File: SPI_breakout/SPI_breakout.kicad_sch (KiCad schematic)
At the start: 2 parts

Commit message: AI assisted edits on board
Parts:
- added J1: OPC-N3 A, Connector_Phoenix_MC:PhoenixContact_MC_1,5_6-G-3.81_1x06_P3.81mm_Horizontal, symbol MyParts:AlphaSense_OPC_N3
- added J2: OPC-N3 B, Connector_Phoenix_MC:PhoenixContact_MC_1,5_6-G-3.81_1x06_P3.81mm_Horizontal, symbol MyParts:AlphaSense_OPC_N3
- added J3: External OPC 5V Input, Connector_Phoenix_MC:PhoenixContact_MC_1,5_2-G-3.81_1x02_P3.81mm_Horizontal, symbol MyParts:External_5V_Input
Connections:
- net SD_CS: now reaches U1.25 (SPI_CS), U2.6 (CS)
- net SPI_CLK: now reaches U1.26 (SPI_CLK), U2.3 (CLK)
- net SPI_CLK: now also J1.6 (SCK), J2.6 (SCK)
- net SPI_MISO: now reaches U1.27 (SPI_MISO), U2.4 (D0_SO)
- net SPI_MISO: now also J1.5 (SDO_MISO), J2.5 (SDO_MISO)
- net SPI_MOSI: now reaches U1.28 (SPI_MOSI), U2.5 (D1_CMD)
- net SPI_MOSI: now also J1.4 (SDI_MOSI), J2.4 (SDI_MOSI)
- net OPC1_CS: now reaches U1.29 (IO1)
- net OPC1_CS: now also J1.3 (SS)
- net OPC2_CS: now reaches U1.31 (IO3)
- net OPC2_CS: now also J2.3 (SS)
- net GND: now reaches U1.40 (GND), U2.2 (GND)
- net GND: now also J1.1 (GND), J2.1 (GND), J3.2 (GND)
- new net OPC_5V_EXT: J1.2 (5V_EXT), J2.2 (5V_EXT), J3.1 (5V_EXT)
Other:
- note added: "J1/J2 pin order: 1 GND black, 2 5V_EXT red, 3 SS green, 4 SDI blue, 5 SDO white, 6 SCK yellow. Use 3.81mm 6-pos pluggable terminals such as TJ0631030000G with a matching PCB header."
- note added: "J3 is the separate OPC 5V input. Pin 1 feeds only OPC_5V_EXT on J1/J2 pin 2; pin 2 ties that supply return to WisBlock GND. It is not tied to the WisBlock 3v3 rail."
- note added: "No level shifter fitted: WisBlock, SD reader, and OPC SPI are expected to use 3.3V logic. Verify OPC SPI adapter before 5V power-up."
- note added: "OPC-N3 5V+ is external; tie the OPC supply ground to WisBlock GND."

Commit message: Reworking routing
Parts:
- added GAS1, GAS2: Screw_Terminal_01x04, MyParts:CONN_1984633_PXC, symbol MyParts:Screw_Terminal_01x04
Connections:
- net GND: now also GAS1.2 (GND)
- net at U1.17 (3v3): now also GAS1.1 (VCC)
- net at U1.19 (SDA1): now also GAS1.4 (SDA)
- net at U1.20 (SCL1): now also GAS1.3 (SCL)
- net at U1.35 (SDA2): now also GAS2.4 (SDA)
- net at U1.36 (SCL2): now also GAS2.3 (SCL)
- net at U1.4 (GND): now also GAS2.2 (GND)
- net at U1.5 (3v3): now also GAS2.1 (VCC)

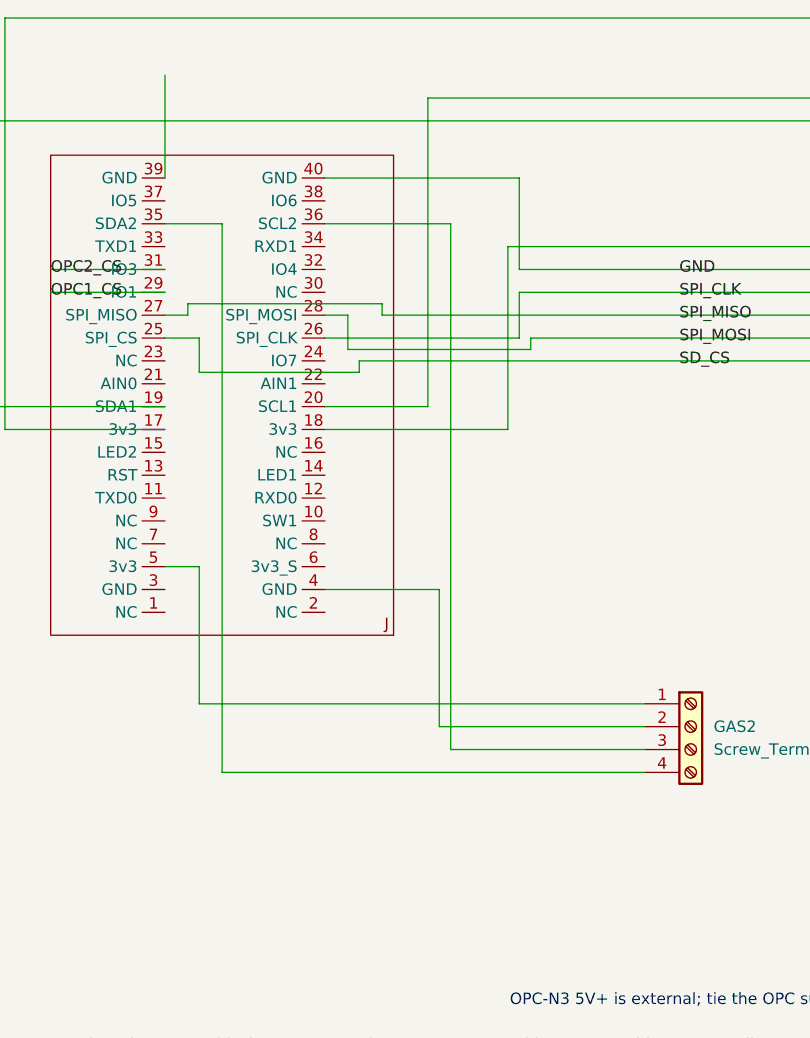
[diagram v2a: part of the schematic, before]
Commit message: Rework into smaller footprint and add 3D models
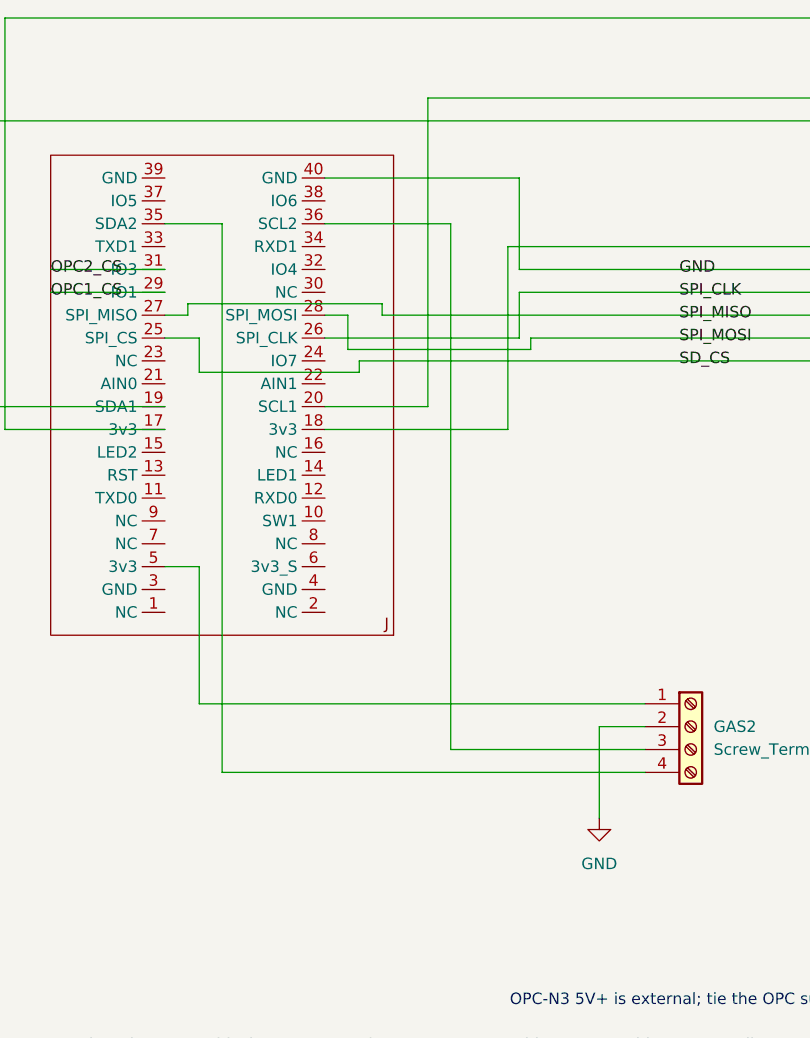
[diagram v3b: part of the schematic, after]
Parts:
- J1, J2: footprint Connector_Phoenix_MC:PhoenixContact_MC_1,5_6-G-3.81_1x06_P3.81mm_Horizontal -> MyParts:CONN_1984659_PXC
- J3: footprint Connector_Phoenix_MC:PhoenixContact_MC_1,5_2-G-3.81_1x02_P3.81mm_Horizontal -> MyParts:CONN_1935161_PXC
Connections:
- net GND: now also GAS2.2 (GND)
- net at U1.4 (GND): no longer GAS2.2 (GND)
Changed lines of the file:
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@@
-	(wire
-		(pts
-			(xy 93.98 93.98) (xy 81.28 93.98)
-		)
-		(stroke
-			(width 0)
-			(type default)
-		)
-	)
 	(wire
 		(pts
@@
 	(wire
 		(pts
-			(xy 63.5 36.83) (xy 63.5 48.26)
-		)
-		(stroke
-			(width 0)
-			(type default)
-		)
-	)
-	(wire
-		(pts
 			(xy 167.64 129.54) (xy 152.4 129.54)
 		)
@@
 	(wire
 		(pts
-			(xy 93.98 109.22) (xy 93.98 93.98)
-		)
-		(stroke
-			(width 0)
-			(type default)
-		)
-	)
-	(wire
-		(pts
 			(xy 63.5 76.2) (xy 45.72 76.2)
 		)
@@
 	(wire
 		(pts
+			(xy 111.76 109.22) (xy 111.76 119.38)
+		)
+		(stroke
+			(width 0)
+			(type default)
+		)
+	)
+	(wire
+		(pts
 			(xy 66.04 63.5) (xy 63.5 63.5)
 		)
@@
 	(wire
 		(pts
+			(xy 116.84 109.22) (xy 111.76 109.22)
+		)
+		(stroke
+			(width 0)
+			(type default)
+		)
+	)
+	(wire
+		(pts
 			(xy 95.25 53.34) (xy 81.28 53.34)
 		)
@@
 		(pts
 			(xy 167.64 55.88) (xy 101.6 55.88)
-		)
-		(stroke
-			(width 0)
-			(type default)
-		)
-	)
-	(wire
-		(pts
-			(xy 116.84 109.22) (xy 93.98 109.22)
 		)
 		(stroke
@@
 			(font
 				(size 1.27 1.27)
+			)
+		)
+	)
+	(symbol
+		(lib_id "power:GND")
+		(at 111.76 119.38 0)
+		(unit 1)
+		(body_style 1)
+		(exclude_from_sim no)
+		(in_bom yes)
+		(on_board yes)
+		(in_pos_files yes)
+		(dnp no)
+		(fields_autoplaced yes)
+		(property "Reference" "#PWR02"
+			(at 111.76 125.73 0)
+			(hide yes)
+			(show_name no)
+			(do_not_autoplace no)
+			(effects
+				(font
+					(size 1.27 1.27)
+				)
+			)
+		)
+		(property "Value" "GND"
+			(at 111.76 124.46 0)
+			(show_name no)
+			(do_not_autoplace no)
+			(effects
+				(font
+					(size 1.27 1.27)
+				)
+			)
+		)
+		(property "Footprint" ""
+			(at 111.76 119.38 0)
+			(hide yes)
+			(show_name no)
+			(do_not_autoplace no)
+			(effects
+				(font
+					(size 1.27 1.27)
+				)
+			)
+		)
+		(property "Datasheet" ""
+			(at 111.76 119.38 0)
+			(hide yes)
+			(show_name no)
+			(do_not_autoplace no)
+			(effects
+				(font
+					(size 1.27 1.27)
+				)
+			)
+		)
+		(property "Description" "Power symbol creates a global label with name \"GND\" , ground"
+			(at 111.76 119.38 0)
+			(hide yes)
+			(show_name no)
+			(do_not_autoplace no)
+			(effects
+				(font
+					(size 1.27 1.27)
+				)
+			)
+		)
+		(pin "1"
+		)
+		(instances
+			(project "SPI_breakout"
+				(path "/d8da890c-b85a-4ee7-8a35-6f5c92ac20f5"
+					(reference "#PWR02")
+					(unit 1)
+				)
 			)
 		)
@@
 			)
 		)
-		(property "Footprint" "Connector_Phoenix_MC:PhoenixContact_MC_1,5_6-G-3.81_1x06_P3.81mm_Horizontal"
+		(property "Footprint" "MyParts:CONN_1984659_PXC"
 			(at 167.64 86.36 0)
 			(hide yes)
@@
 			)
 		)
-		(property "Footprint" "Connector_Phoenix_MC:PhoenixContact_MC_1,5_6-G-3.81_1x06_P3.81mm_Horizontal"
+		(property "Footprint" "MyParts:CONN_1984659_PXC"
 			(at 167.64 114.3 0)
 			(hide yes)
@@
 			)
 		)
-		(property "Footprint" "Connector_Phoenix_MC:PhoenixContact_MC_1,5_2-G-3.81_1x02_P3.81mm_Horizontal"
+		(property "Footprint" "MyParts:CONN_1935161_PXC"
 			(at 167.64 157.48 0)
 			(hide yes)

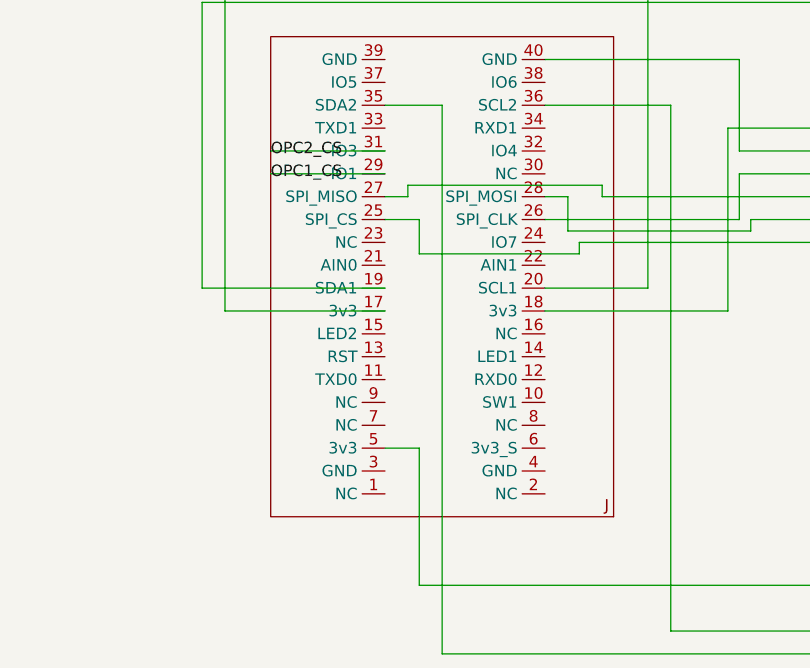
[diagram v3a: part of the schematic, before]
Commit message: Cleaning up routes
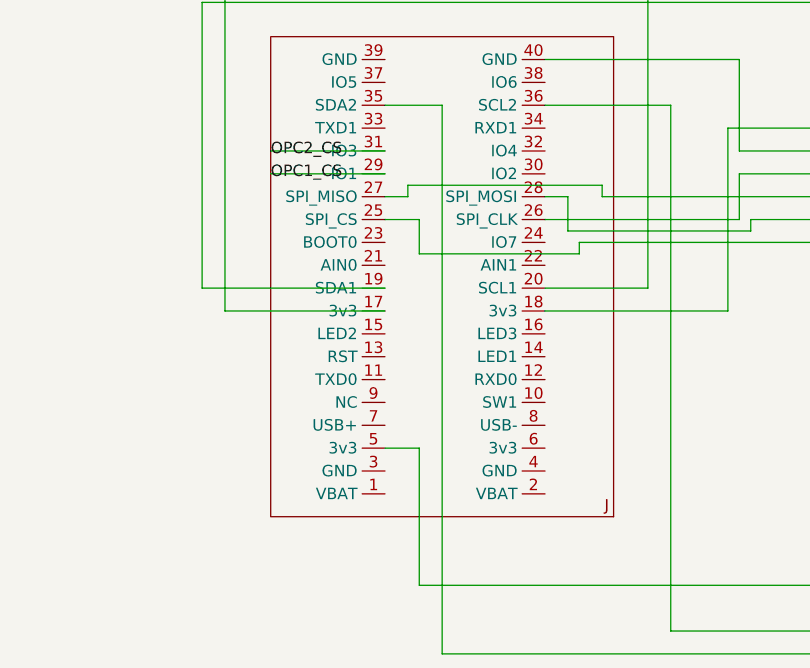
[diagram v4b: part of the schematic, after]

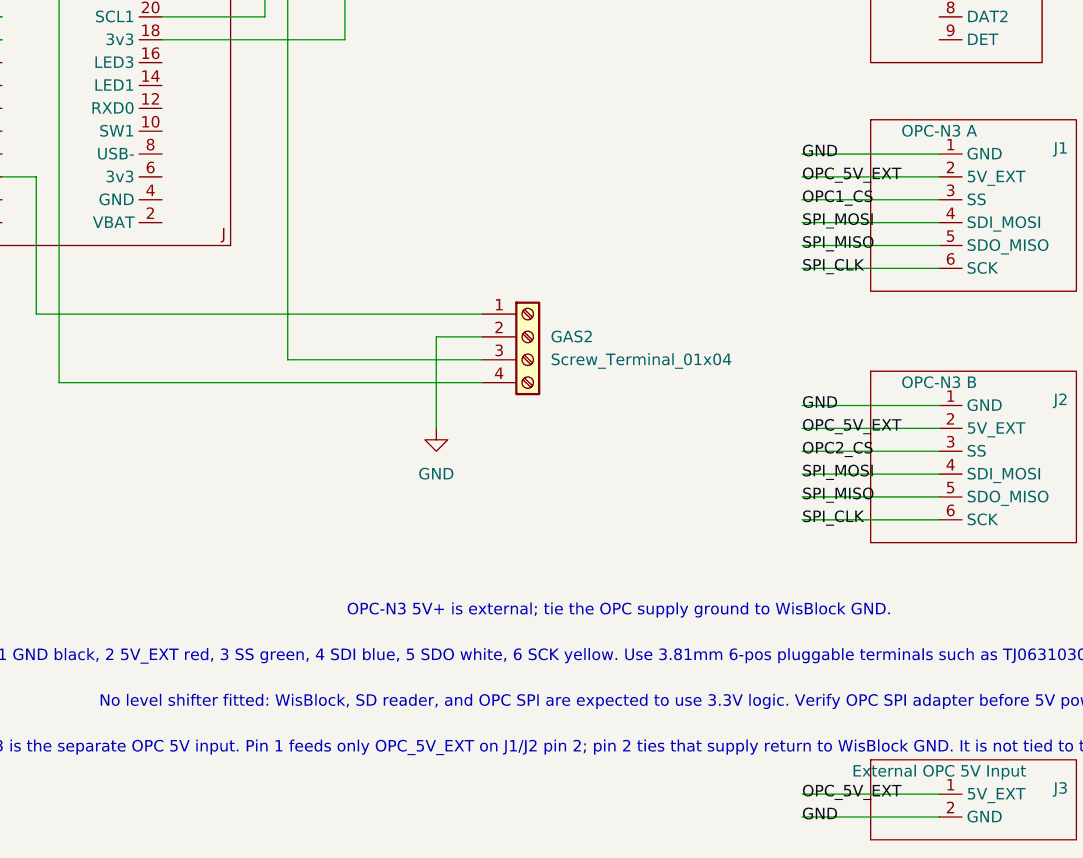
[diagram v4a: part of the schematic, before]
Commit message: Added power switching and bigger pad for SD mount
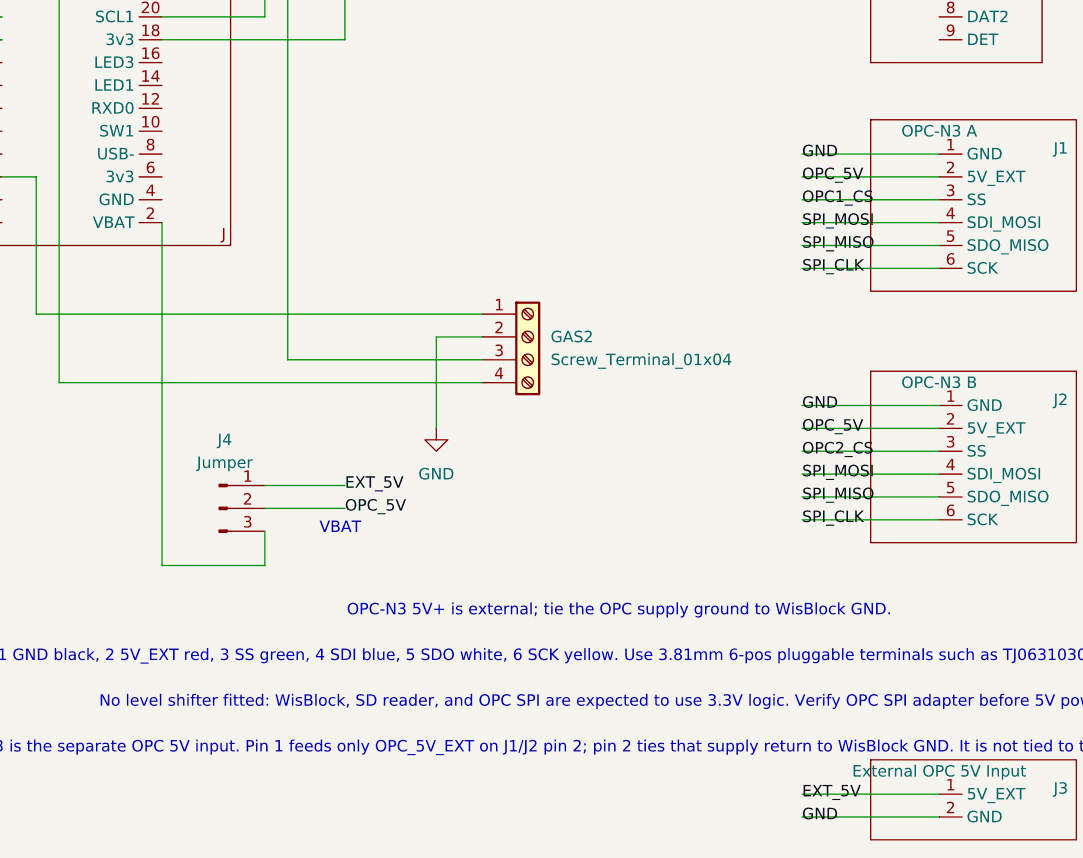
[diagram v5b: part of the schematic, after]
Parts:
- added J4: Jumper, Connector_PinHeader_2.54mm:PinHeader_1x03_P2.54mm_Vertical, symbol MyParts:Jumper
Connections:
- net at U1.2 (VBAT): now also J4.3 (VBAT)
- net OPC_5V_EXT renamed OPC_5V
- net OPC_5V: now also J4.2 (OPC_5V); no longer J3.1 (5V_EXT)
- new net EXT_5V: J3.1 (5V_EXT), J4.1 (EXT_5V)
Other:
- note added: "VBAT"
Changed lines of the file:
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@@
+		)
+	)
+	(text "VBAT"
+		(exclude_from_sim no)
+		(at 101.092 130.556 0)
+		(effects
+			(font
+				(size 1.27 1.27)
+				(color 0 0 0 1)
+			)
 		)
 	)
@@
 	(wire
 		(pts
+			(xy 92.71 134.62) (xy 92.71 130.81)
+		)
+		(stroke
+			(width 0)
+			(type default)
+		)
+	)
+	(wire
+		(pts
 			(xy 167.64 68.58) (xy 85.09 68.58)
 		)
@@
 	(wire
 		(pts
+			(xy 81.28 134.62) (xy 92.71 134.62)
+		)
+		(stroke
+			(width 0)
+			(type default)
+		)
+	)
+	(wire
+		(pts
 			(xy 167.64 66.04) (xy 104.14 66.04)
 		)
@@
 	(wire
 		(pts
+			(xy 92.71 125.73) (xy 101.6 125.73)
+		)
+		(stroke
+			(width 0)
+			(type default)
+		)
+	)
+	(wire
+		(pts
 			(xy 83.82 63.5) (xy 81.28 63.5)
 		)
@@
 	(wire
 		(pts
+			(xy 92.71 128.27) (xy 101.6 128.27)
+		)
+		(stroke
+			(width 0)
+			(type default)
+		)
+	)
+	(wire
+		(pts
 			(xy 83.82 67.31) (xy 83.82 63.5)
 		)
@@
 		(pts
 			(xy 43.18 41.91) (xy 43.18 73.66)
+		)
+		(stroke
+			(width 0)
+			(type default)
+		)
+	)
+	(wire
+		(pts
+			(xy 81.28 96.52) (xy 81.28 134.62)
 		)
 		(stroke
@@
 		)
 	)
+	(label "OPC_5V"
+		(at 101.6 128.27 0)
+		(effects
+			(font
+				(size 1.27 1.27)
+			)
+		)
+	)
 	(label "OPC1_CS"
 		(at 152.4 93.98 0)
@@
 		)
 	)
-	(label "OPC_5V_EXT"
+	(label "EXT_5V"
 		(at 152.4 160.02 0)
 		(effects
@@
 		)
 	)
-	(label "OPC_5V_EXT"
+	(label "OPC_5V"
 		(at 152.4 119.38 0)
 		(effects
@@
 		)
 	)
-	(label "OPC_5V_EXT"
+	(label "EXT_5V"
+		(at 101.6 125.73 0)
+		(effects
+			(font
+				(size 1.27 1.27)
+			)
+		)
+	)
+	(label "OPC_5V"
 		(at 152.4 91.44 0)
 		(effects
@@
 					(unit 1)
 				)
+			)
+		)
+	)
+	(symbol
+		(lib_id "MyParts:Jumper")
+		(at 87.63 128.27 0)
+		(unit 1)
+		(body_style 1)
+		(exclude_from_sim no)
+		(in_bom yes)
+		(on_board yes)
+		(in_pos_files yes)
+		(dnp no)
+		(fields_autoplaced yes)
+		(property "Reference" "J4"
+			(at 88.265 120.65 0)
+			(show_name no)
+			(do_not_autoplace no)
+			(effects
+				(font
+					(size 1.27 1.27)
+				)
+			)
+		)
+		(property "Value" "Jumper"
+			(at 88.265 123.19 0)
+			(show_name no)
+			(do_not_autoplace no)
+			(effects
+				(font
+					(size 1.27 1.27)
+				)
+			)
+		)
+		(property "Footprint" "Connector_PinHeader_2.54mm:PinHeader_1x03_P2.54mm_Vertical"
+			(at 87.63 128.27 0)
+			(hide yes)
+			(show_name no)
+			(do_not_autoplace no)
+			(effects
+				(font
+					(size 1.27 1.27)
+				)
+			)
+		)
+		(property "Datasheet" ""
+			(at 87.63 128.27 0)
+			(hide yes)
+			(show_name no)
+			(do_not_autoplace no)
+			(effects
+				(font
+					(size 1.27 1.27)
+				)
+			)
+		)
+		(property "Description" "01x03 Pin Jumper"
+			(at 98.552 122.936 0)
+			(hide yes)
+			(show_name no)
+			(do_not_autoplace no)
+			(effects
+				(font
+					(size 1.27 1.27)
+				)
+			)
+		)
+		(pin "1"
+		)
+		(pin "2"
+		)
+		(pin "3"
+		)
+		(instances
+			(project "SPI_breakout"
+				(path "/d8da890c-b85a-4ee7-8a35-6f5c92ac20f5"
+					(reference "J4")
+					(unit 1)
+				)

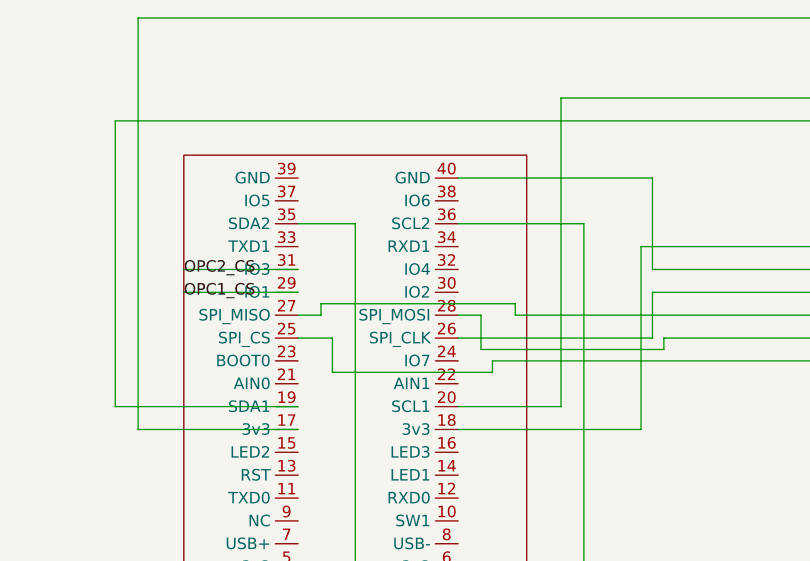
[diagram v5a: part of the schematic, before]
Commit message: Change IO pin to 2 to avoid GPS conflict
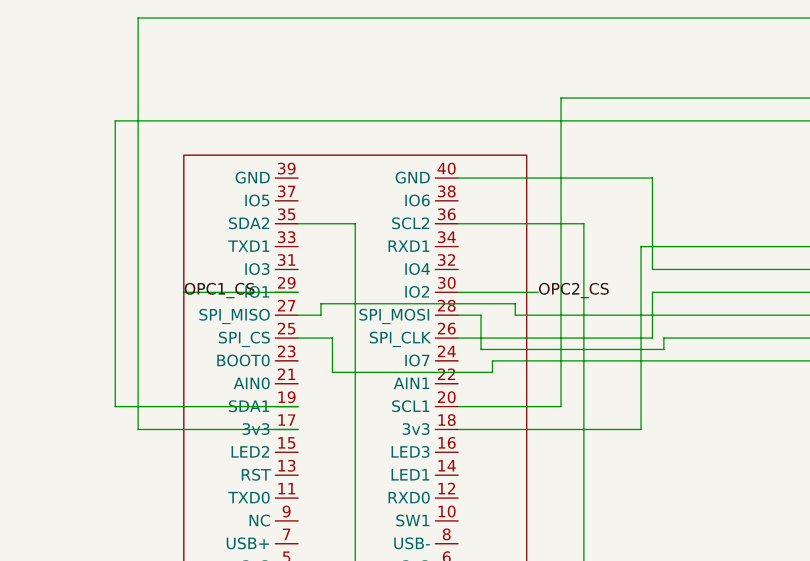
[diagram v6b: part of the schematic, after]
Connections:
- net OPC2_CS: now also U1.30 (IO2); no longer U1.31 (IO3)
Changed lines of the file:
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@@
-	(wire
-		(pts
-			(xy 63.5 58.42) (xy 50.8 58.42)
-		)
-		(stroke
-			(width 0)
-			(type default)
-		)
-	)
 	(wire
 		(pts
@@
 		(pts
 			(xy 167.64 88.9) (xy 152.4 88.9)
+		)
+		(stroke
+			(width 0)
+			(type default)
+		)
+	)
+	(wire
+		(pts
+			(xy 81.28 60.96) (xy 90.17 60.96)
 		)
 		(stroke
@@
 	)
 	(label "OPC2_CS"
-		(at 50.8 58.42 0)
-		(effects
-			(font
+		(at 90.17 60.96 0)
+		(effects
+			(font

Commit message: Final checks
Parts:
- J1, J2: footprint MyParts:CONN_1984659_PXC -> Connector_Phoenix_MC:PhoenixContact_MC_1,5_6-G-3.81_1x06_P3.81mm_Horizontal
- J3: footprint MyParts:CONN_1935161_PXC -> Connector_Phoenix_MC:PhoenixContact_MC_1,5_2-G-3.81_1x02_P3.81mm_Horizontal
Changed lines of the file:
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@@
 			)
 		)
-		(property "Footprint" "MyParts:CONN_1984659_PXC"
+		(property "Footprint" "Connector_Phoenix_MC:PhoenixContact_MC_1,5_6-G-3.81_1x06_P3.81mm_Horizontal"
 			(at 167.64 86.36 0)
 			(hide yes)
@@
 			)
 		)
-		(property "Footprint" "MyParts:CONN_1984659_PXC"
+		(property "Footprint" "Connector_Phoenix_MC:PhoenixContact_MC_1,5_6-G-3.81_1x06_P3.81mm_Horizontal"
 			(at 167.64 114.3 0)
 			(hide yes)
@@
 			)
 		)
-		(property "Footprint" "MyParts:CONN_1935161_PXC"
+		(property "Footprint" "Connector_Phoenix_MC:PhoenixContact_MC_1,5_2-G-3.81_1x02_P3.81mm_Horizontal"
 			(at 167.64 157.48 0)
 			(hide yes)
